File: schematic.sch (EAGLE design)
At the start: 42 parts, among them U1 ADP3338AKCZ-3.3RL7

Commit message: Made the two layer board.
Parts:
- added UART: (no value), SparkFun-Connectors:M03LONGPADS
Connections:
- net GND: now also UART.3
- net RX: now also UART.1
- net TX: now also UART.2
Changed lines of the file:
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@@
 <part name="D12" library="SparkFun-LED" deviceset="LED-RED" device="1206" value="RED"/>
 <part name="D13" library="SparkFun-LED" deviceset="LED-RED" device="1206" value="RED"/>
+<part name="UART" library="SparkFun-Connectors" deviceset="M03" device="LONGPADS"/>
 </parts>
 <sheets>
@@
 <instance part="D12" gate="G$1" x="-7.62" y="-114.3" rot="R270"/>
 <instance part="D13" gate="G$1" x="-7.62" y="-124.46" rot="R270"/>
+<instance part="UART" gate="G$1" x="-33.02" y="55.88" rot="R270"/>
 </instances>
 <busses>
@@
 <label x="-35.56" y="-99.06" size="1.778" layer="95"/>
 </segment>
+<segment>
+<pinref part="UART" gate="G$1" pin="3"/>
+<wire x1="-30.48" y1="48.26" x2="-30.48" y2="43.18" width="0.1524" layer="91"/>
+<label x="-30.48" y="43.18" size="1.778" layer="95" rot="R90"/>
+</segment>
 </net>
 <net name="M1" class="0">
@@
 <label x="20.32" y="-66.04" size="1.778" layer="95"/>
 </segment>
+<segment>
+<pinref part="UART" gate="G$1" pin="2"/>
+<wire x1="-33.02" y1="48.26" x2="-33.02" y2="43.18" width="0.1524" layer="91"/>
+<label x="-33.02" y="43.18" size="1.778" layer="95" rot="R90"/>
+</segment>
 </net>
 <net name="RX" class="0">
@@
 <label x="167.64" y="-20.32" size="1.778" layer="95"/>
 </segment>
-</net>
+<segment>
+<pinref part="UART" gate="G$1" pin="1"/>
+<wire x1="-35.56" y1="48.26" x2="-35.56" y2="43.18" width="0.1524" layer="91"/>
+<label x="-35.56" y="43.18" size="1.778" layer="95" rot="R90"/>
+</segment>
+</net>

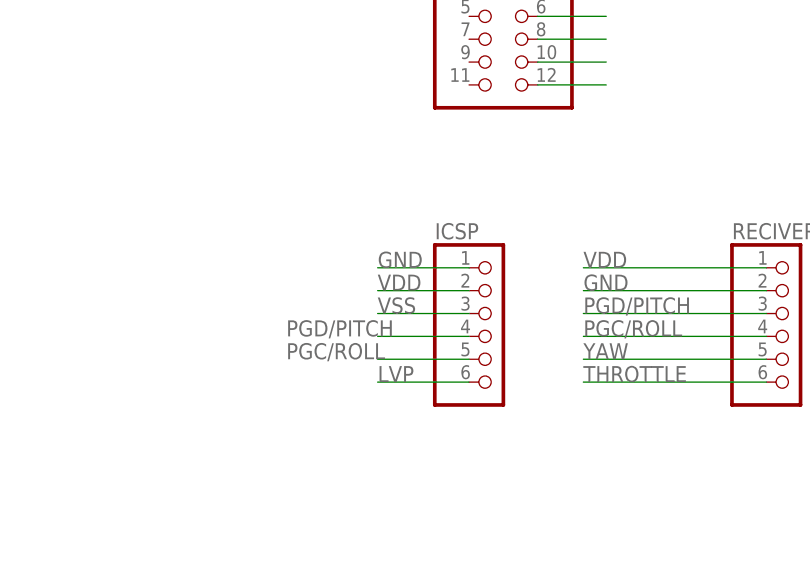
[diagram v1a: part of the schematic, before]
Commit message: Fixed a mixup in the pinout for the ICSP
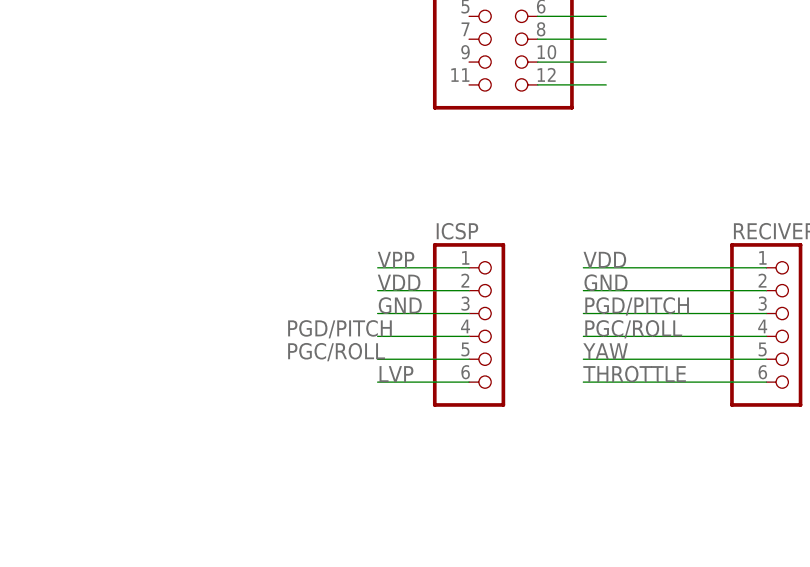
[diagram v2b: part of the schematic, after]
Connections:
- removed net VSS: ICSP.3
- net GND: now also ICSP.3; no longer ICSP.1
- net VPP: now also ICSP.1
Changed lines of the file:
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@@
 <label x="-11.176" y="-11.938" size="1.778" layer="95"/>
+</segment>
+<segment>
+<label x="86.36" y="53.34" size="1.778" layer="95"/>
+<pinref part="ICSP" gate="A" pin="1"/>
+<wire x1="86.36" y1="53.34" x2="96.52" y2="53.34" width="0.1524" layer="91"/>
 </segment>
 </net>
@@
 </segment>
 </net>
-<net name="VSS" class="0">
-<segment>
-<label x="86.36" y="48.26" size="1.778" layer="95"/>
-<pinref part="ICSP" gate="A" pin="3"/>
-<wire x1="86.36" y1="48.26" x2="96.52" y2="48.26" width="0.1524" layer="91"/>
-</segment>
-</net>
 <net name="LVP" class="0">
 <segment>
@@
 <wire x1="33.02" y1="33.02" x2="33.02" y2="27.94" width="0.1524" layer="91"/>
 <label x="30.48" y="25.4" size="1.778" layer="95"/>
-</segment>
-<segment>
-<label x="86.36" y="53.34" size="1.778" layer="95"/>
-<pinref part="ICSP" gate="A" pin="1"/>
-<wire x1="86.36" y1="53.34" x2="96.52" y2="53.34" width="0.1524" layer="91"/>
 </segment>
 <segment>
@@
 <label x="-30.48" y="43.18" size="1.778" layer="95" rot="R90"/>
 </segment>
-</net>
+<segment>
+<label x="86.36" y="48.26" size="1.778" layer="95"/>
+<pinref part="ICSP" gate="A" pin="3"/>
+<wire x1="86.36" y1="48.26" x2="96.52" y2="48.26" width="0.1524" layer="91"/>
+</segment>
+</net>

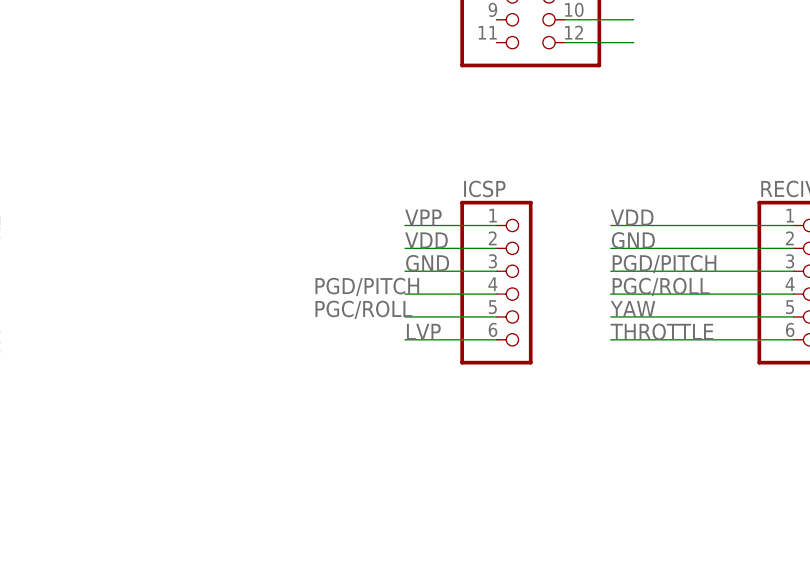
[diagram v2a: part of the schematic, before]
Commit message: Reversed ICSP pins so programmer will be right way up
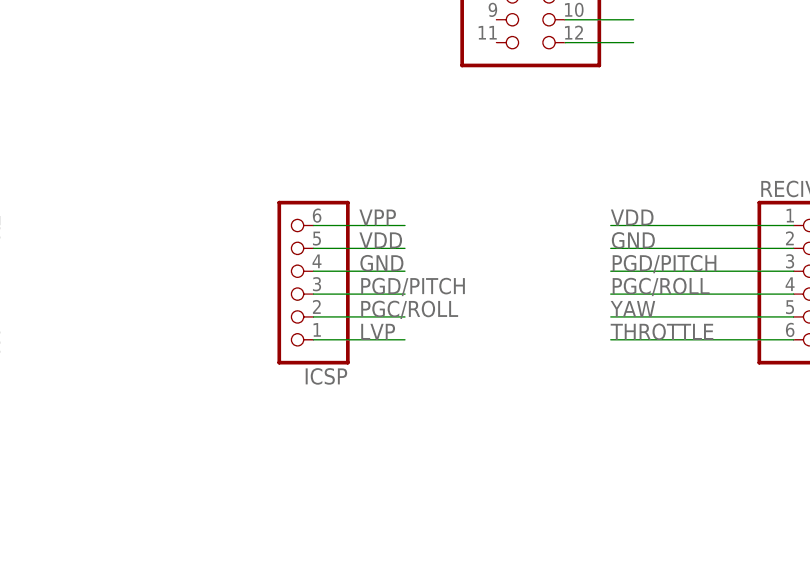
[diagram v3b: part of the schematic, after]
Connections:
- net GND: now also ICSP.4; no longer ICSP.3
- net LVP: now also ICSP.1; no longer ICSP.6
- net PGC/ROLL: now also ICSP.2; no longer ICSP.5
- net PGD/PITCH: now also ICSP.3; no longer ICSP.4
- net VDD: now also ICSP.5; no longer ICSP.2
- net VPP: now also ICSP.6; no longer ICSP.1
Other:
- moved on the sheet: ICSP
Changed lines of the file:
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@@
 <instance part="R5" gate="G$1" x="27.94" y="38.1" rot="R270"/>
 <instance part="U1" gate="A" x="170.18" y="48.26"/>
-<instance part="ICSP" gate="A" x="99.06" y="45.72"/>
+<instance part="ICSP" gate="A" x="73.66" y="48.26" rot="R180"/>
 <instance part="ESC" gate="A" x="99.06" y="81.28"/>
 <instance part="RECIVER" gate="A" x="132.08" y="45.72"/>
@@
 </segment>
 <segment>
-<label x="86.36" y="53.34" size="1.778" layer="95"/>
-<pinref part="ICSP" gate="A" pin="1"/>
-<wire x1="86.36" y1="53.34" x2="96.52" y2="53.34" width="0.1524" layer="91"/>
+<pinref part="ICSP" gate="A" pin="6"/>
+<wire x1="76.2" y1="53.34" x2="86.36" y2="53.34" width="0.1524" layer="91"/>
+<label x="81.28" y="53.34" size="1.778" layer="95"/>
 </segment>
 </net>
@@
 </segment>
 <segment>
-<pinref part="ICSP" gate="A" pin="2"/>
-<wire x1="86.36" y1="50.8" x2="96.52" y2="50.8" width="0.1524" layer="91"/>
-<label x="86.36" y="50.8" size="1.778" layer="95"/>
-</segment>
-<segment>
 <pinref part="RECIVER" gate="A" pin="1"/>
 <wire x1="129.54" y1="53.34" x2="109.22" y2="53.34" width="0.1524" layer="91"/>
@@
 <label x="68.58" y="-154.94" size="1.778" layer="95"/>
 </segment>
-</net>
-<net name="LVP" class="0">
-<segment>
-<label x="86.36" y="40.64" size="1.778" layer="95"/>
-<pinref part="ICSP" gate="A" pin="6"/>
-<wire x1="86.36" y1="40.64" x2="96.52" y2="40.64" width="0.1524" layer="91"/>
+<segment>
+<pinref part="ICSP" gate="A" pin="5"/>
+<wire x1="76.2" y1="50.8" x2="86.36" y2="50.8" width="0.1524" layer="91"/>
+<label x="81.28" y="50.8" size="1.778" layer="95"/>
 </segment>
 </net>
@@
 </segment>
 <segment>
-<label x="86.36" y="48.26" size="1.778" layer="95"/>
-<pinref part="ICSP" gate="A" pin="3"/>
-<wire x1="86.36" y1="48.26" x2="96.52" y2="48.26" width="0.1524" layer="91"/>
+<pinref part="ICSP" gate="A" pin="4"/>
+<wire x1="76.2" y1="48.26" x2="86.36" y2="48.26" width="0.1524" layer="91"/>
+<label x="81.28" y="48.26" size="1.778" layer="95"/>
 </segment>
 </net>
@@
 <net name="PGD/PITCH" class="0">
 <segment>
-<label x="76.2" y="45.72" size="1.778" layer="95"/>
-<pinref part="ICSP" gate="A" pin="4"/>
-<wire x1="86.36" y1="45.72" x2="96.52" y2="45.72" width="0.1524" layer="91"/>
-</segment>
-<segment>
 <pinref part="RECIVER" gate="A" pin="3"/>
 <wire x1="129.54" y1="48.26" x2="109.22" y2="48.26" width="0.1524" layer="91"/>
@@
 <label x="167.64" y="-2.54" size="1.778" layer="95"/>
 </segment>
+<segment>
+<pinref part="ICSP" gate="A" pin="3"/>
+<wire x1="76.2" y1="45.72" x2="86.36" y2="45.72" width="0.1524" layer="91"/>
+<label x="81.28" y="45.72" size="1.778" layer="95"/>
+</segment>
 </net>
 <net name="PGC/ROLL" class="0">
@@
 </segment>
 <segment>
-<pinref part="ICSP" gate="A" pin="5"/>
-<wire x1="86.36" y1="43.18" x2="96.52" y2="43.18" width="0.1524" layer="91"/>
-<label x="76.2" y="43.18" size="1.778" layer="95"/>
+<pinref part="ICSP" gate="A" pin="2"/>
+<wire x1="76.2" y1="43.18" x2="86.36" y2="43.18" width="0.1524" layer="91"/>
+<label x="81.28" y="43.18" size="1.778" layer="95"/>
 </segment>
 </net>
@@
 </segment>
 </net>
+<net name="LVP" class="0">
+<segment>
+<pinref part="ICSP" gate="A" pin="1"/>
+<wire x1="76.2" y1="40.64" x2="86.36" y2="40.64" width="0.1524" layer="91"/>
+<label x="81.28" y="40.64" size="1.778" layer="95"/>
+</segment>
+</net>
